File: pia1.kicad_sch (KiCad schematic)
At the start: 35 parts, among them IC20 MC14529B, IC24 74LS244N, IC25 LM393P, IC26 MC6821, IC31 74LS02N

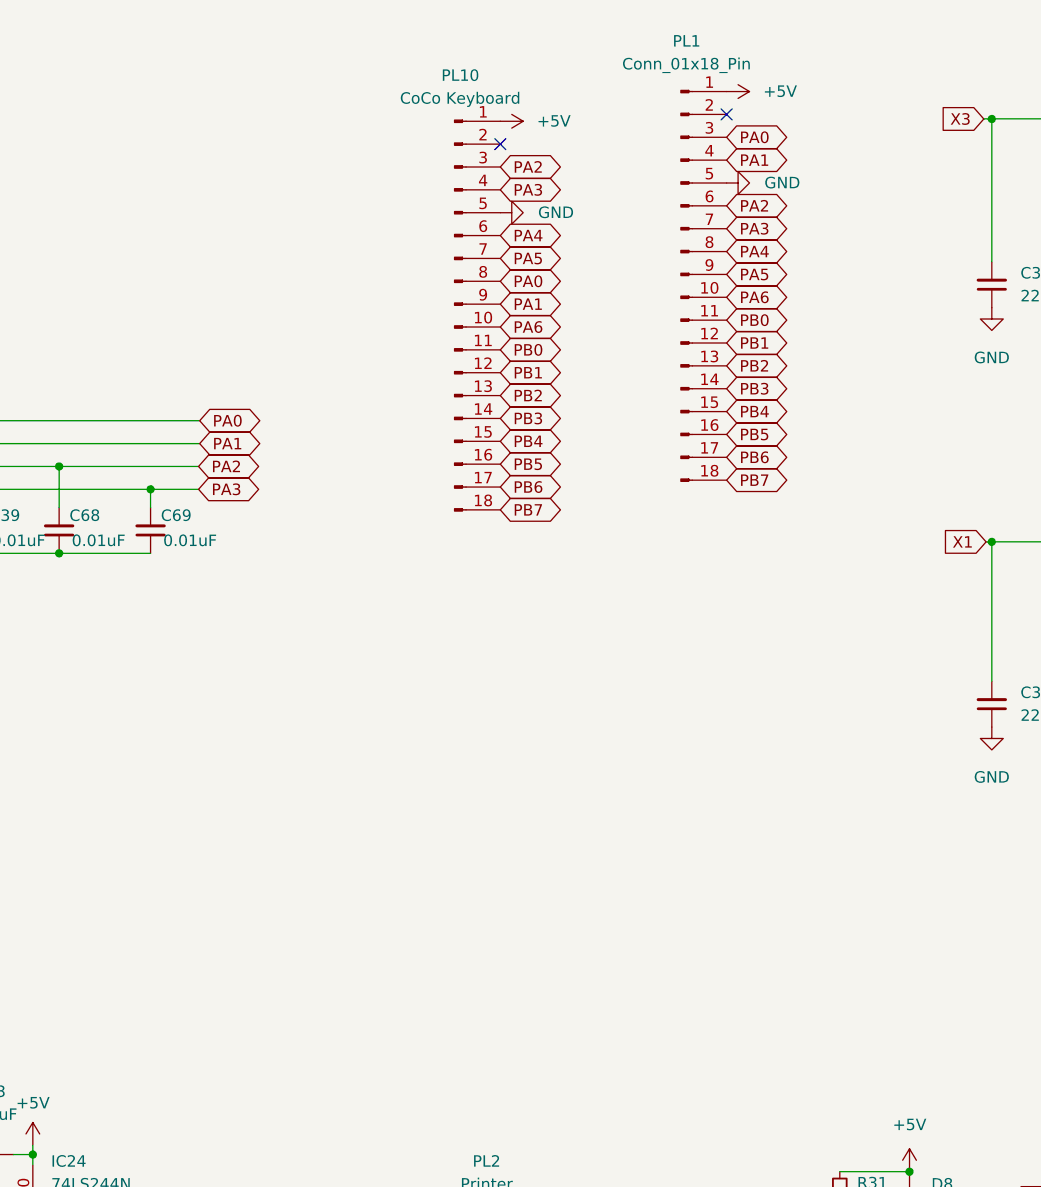
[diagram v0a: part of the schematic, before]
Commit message: update to keyboard switch option
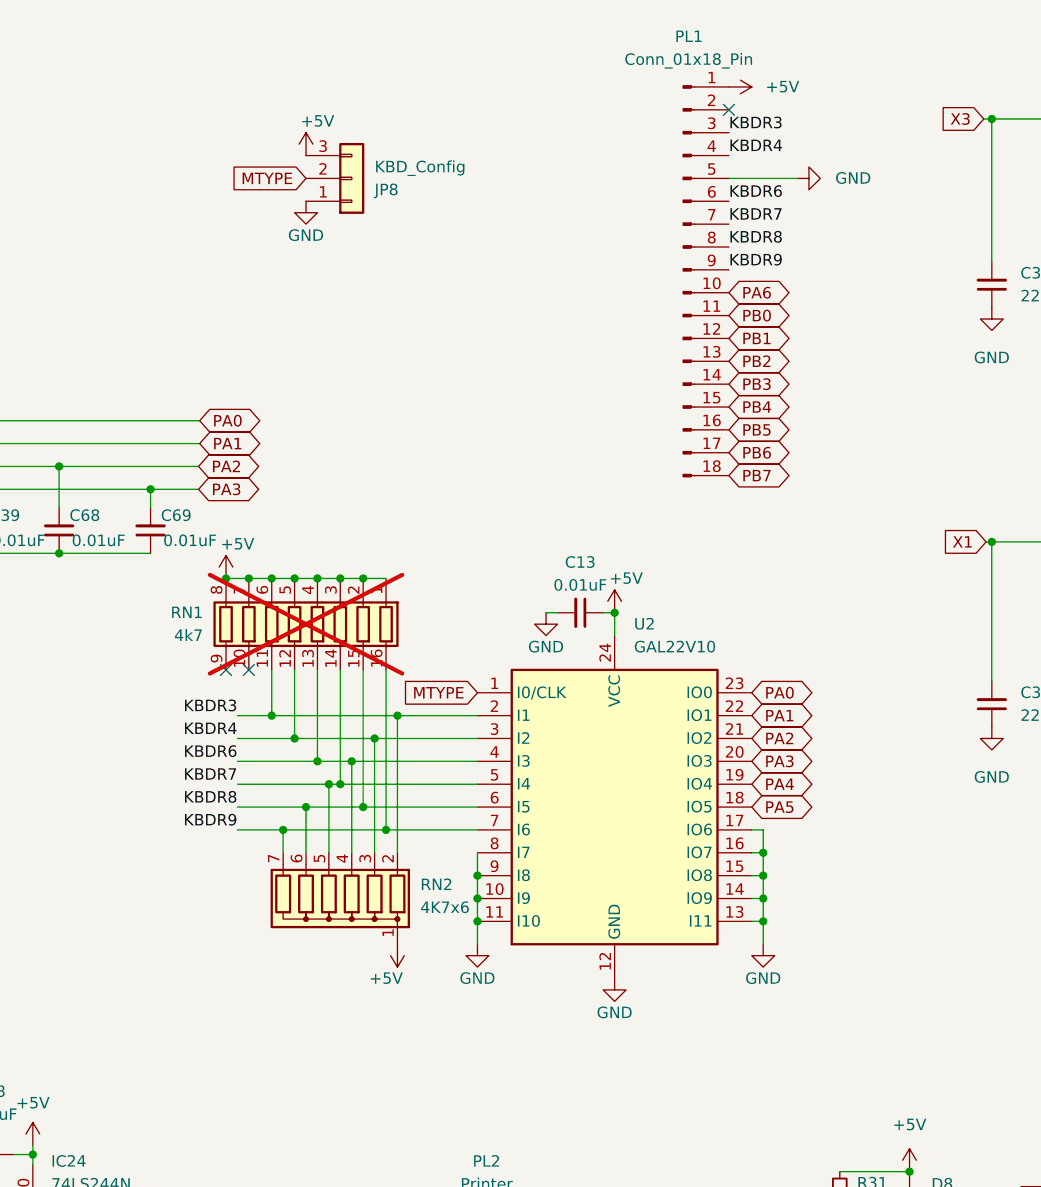
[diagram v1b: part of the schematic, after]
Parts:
- removed PL10: CoCo Keyboard, Connector_PinHeader_2.54mm:PinHeader_1x18_P2.54mm_Vertical, symbol Connector:Conn_01x18_Pin
- added C13: 0.01uF, Capacitor_THT:C_Disc_D4.3mm_W1.9mm_P5.00mm, symbol Device:C_Small
- added JP8: KBD_Config, Connector_PinHeader_2.54mm:PinHeader_1x03_P2.54mm_Vertical, symbol Connector_Generic:Conn_01x03
- added RN1: 4k7, PCM_Resistor_SMD_AKL:R_Array_Convex_8x0602, symbol PCM_Resistor_AKL:R_8x0602_Convex
- added RN2: 4K7x6, Resistor_THT:R_Array_SIP7, symbol Device:R_Network06
- added U2: GAL22V10, Package_DIP:DIP-24_W7.62mm, symbol vdg:GAL22V10
- C30, C31, C32, C33: LCSC (none) -> C1729
- IC24: LCSC (none) -> C22374098
- IC25: LCSC (none) -> C5209
- IC31: LCSC (none) -> C22374091; SA2120 Sheet 1 (spare) -> (none)
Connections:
- net +5V: now also C13.1, JP8.3 (Pin_3), RN1.1 (R1.1), RN1.2 (R2.1), RN1.3 (R3.1), RN1.4 (R4.1), RN1.5 (R5.1), RN1.6 (R6.1), RN1.7 (R7.1), RN1.8 (R8.1), RN2.1 (common), U2.24 (VCC)
- net GND: now also C13.2, JP8.1 (Pin_1), U2.10 (I9), U2.11 (I10), U2.12 (GND), U2.13 (I11), U2.14 (IO9), U2.15 (IO8), U2.16 (IO7), U2.17 (IO6), U2.8 (I7), U2.9 (I8)
- net PA0: now also U2.23 (IO0); no longer PL1.3 (Pin_3)
- net PA1: now also U2.22 (IO1); no longer PL1.4 (Pin_4)
- net PA2: now also U2.21 (IO2); no longer PL1.6 (Pin_6)
- net PA3: now also U2.20 (IO3); no longer PL1.7 (Pin_7)
- net PA4: now also U2.19 (IO4); no longer PL1.8 (Pin_8)
- net PA5: now also U2.18 (IO5); no longer PL1.9 (Pin_9)
- new net KBDR3: PL1.3 (Pin_3), RN1.11 (R6.2), RN2.2 (R1), U2.2 (I1)
- new net KBDR4: PL1.4 (Pin_4), RN1.12 (R5.2), RN2.3 (R2), U2.3 (I2)
- new net KBDR6: PL1.6 (Pin_6), RN1.13 (R4.2), RN2.4 (R3), U2.4 (I3)
- new net KBDR7: PL1.7 (Pin_7), RN1.14 (R3.2), RN2.5 (R4), U2.5 (I4)
- new net KBDR8: PL1.8 (Pin_8), RN1.15 (R2.2), RN2.6 (R5), U2.6 (I5)
- new net KBDR9: PL1.9 (Pin_9), RN1.16 (R1.2), RN2.7 (R6), U2.7 (I6)
- new net MTYPE: JP8.2 (Pin_2), U2.1 (I0/CLK)
- no-connect marks 2 -> 3
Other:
- title: (none) -> Dragon CPU UK Revised
- moved on the sheet: PL1
